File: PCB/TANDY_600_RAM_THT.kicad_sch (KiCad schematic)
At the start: 5 parts, among them J1 DIN 41612 2x22 male right-ang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, U1 628128, U2 74HC08

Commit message: dual_008
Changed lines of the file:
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@@
   )
   (label "A16" (at 140.97 109.22 0)
-    (effects (font (size 1.524 1.524)) (justify left bottom))
+    (effects (font (size 1.27 1.27)) (justify left bottom))
   )
   (label "A14" (at 66.04 58.42 180)
@@
   )
   (label "A15" (at 140.97 96.52 0)
-    (effects (font (size 1.524 1.524)) (justify left bottom))
+    (effects (font (size 1.27 1.27)) (justify left bottom))
   )
   (label "D3" (at 209.55 66.04 0)

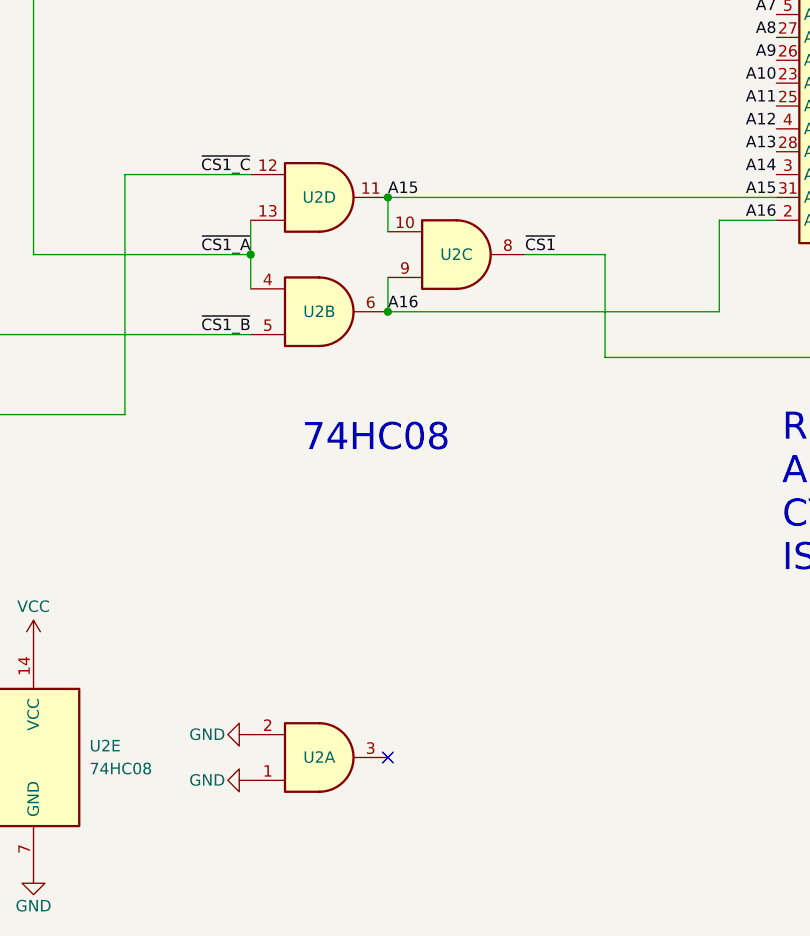
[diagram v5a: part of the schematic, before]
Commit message: dual version add /CE pullup for battery life
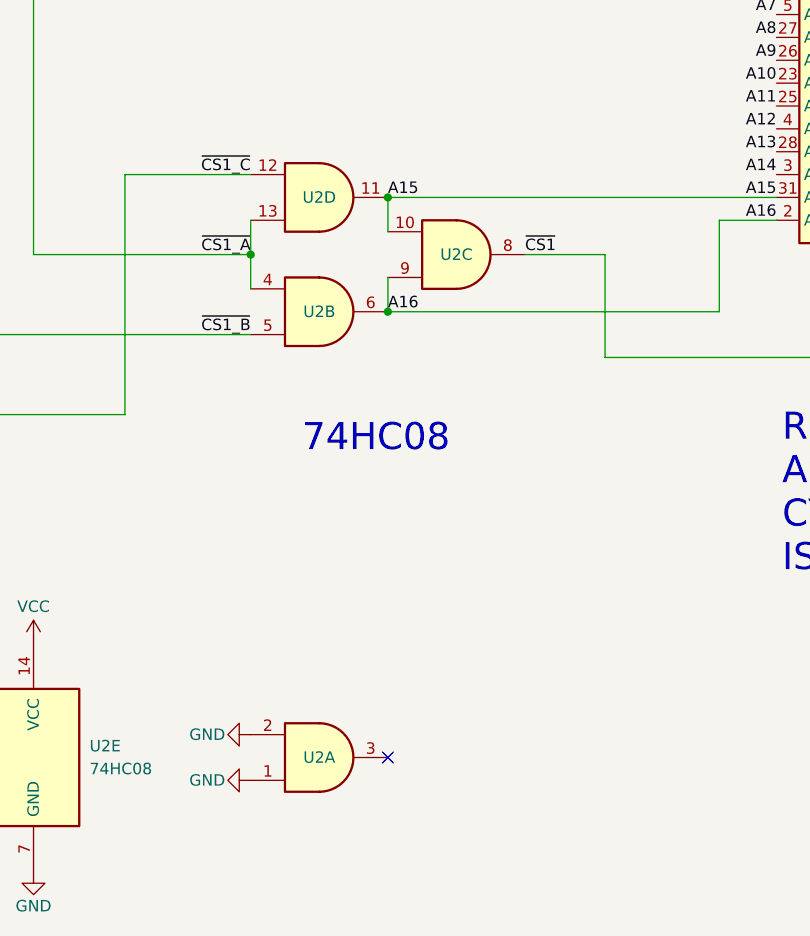
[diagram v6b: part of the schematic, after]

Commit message: datasheets OPRM pinout
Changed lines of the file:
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@@
 (kicad_sch
-	(version 20231120)
+	(version 20250114)
 	(generator "eeschema")
-	(generator_version "8.0")
+	(generator_version "9.0")
 	(paper "USLetter")
 	(title_block
@@
 		(comment 3 "Replaces TANDY Cat. No. 26-3910 \"OPRM\"")
 	)
+	(text "~{RAM_BACKUP}"
+		(exclude_from_sim no)
+		(at 83.82 101.6 0)
+		(effects
+			(font
+				(size 1.27 1.27)
+			)
+			(justify left bottom)
+		)
+	)
+	(text "74HC08"
+		(exclude_from_sim no)
+		(at 131.445 125.095 0)
+		(effects
+			(font
+				(size 3 3)
+			)
+			(justify left bottom)
+		)
+	)
+	(text "R1LP0108E\nAS6C1008\nCY62128ELL\nIS62C1024AL\n"
+		(exclude_from_sim no)
+		(at 184.785 138.43 0)
+		(effects
+			(font
+				(size 3 3)
+			)
+			(justify left bottom)
+		)
+	)
 	(junction
 		(at 125.73 102.87)
@@
 		)
 	)
-	(text "~{RAM_BACKUP}"
-		(exclude_from_sim no)
-		(at 83.82 101.6 0)
-		(effects
-			(font
-				(size 1.27 1.27)
-			)
-			(justify left bottom)
-		)
-	)
-	(text "74HC08"
-		(exclude_from_sim no)
-		(at 131.445 125.095 0)
-		(effects
-			(font
-				(size 3 3)
-			)
-			(justify left bottom)
-		)
-	)
-	(text "R1LP0108E\nAS6C1008\nCY62128ELL\nIS62C1024AL\n"
-		(exclude_from_sim no)
-		(at 184.785 138.43 0)
-		(effects
-			(font
-				(size 3 3)
-			)
-			(justify left bottom)
-		)
-	)
 	(label "D2"
 		(at 78.74 88.9 0)
-		(fields_autoplaced yes)
 		(effects
 			(font
@@
 	(label "~{CS1_C}"
 		(at 66.04 99.06 180)
-		(fields_autoplaced yes)
 		(effects
 			(font
@@
 	(label "A13"
 		(at 78.74 58.42 0)
-		(fields_autoplaced yes)
 		(effects
 			(font
@@
 	(label "A12"
 		(at 66.04 60.96 180)
-		(fields_autoplaced yes)
 		(effects
 			(font
@@
 	(label "D6"
 		(at 66.04 83.82 180)
-		(fields_autoplaced yes)
 		(effects
 			(font
@@
 	(label "A13"
 		(at 184.15 91.44 180)
-		(fields_autoplaced yes)
 		(effects
 			(font
@@
 	(label "A7"
 		(at 184.15 76.2 180)
-		(fields_autoplaced yes)
 		(effects
 			(font
@@
 	(label "A1"
 		(at 184.15 60.96 180)
-		(fields_autoplaced yes)
 		(effects
 			(font
@@
 	(label "~{WE}"
 		(at 209.55 88.9 0)
-		(fields_autoplaced yes)
 		(effects
 			(font
@@
 	(label "A4"
 		(at 66.04 73.66 180)
-		(fields_autoplaced yes)
 		(effects
 			(font
@@
 	(label "A3"
 		(at 66.04 76.2 180)
-		(fields_autoplaced yes)
 		(effects
 			(font
@@
 	(label "A4"
 		(at 184.15 68.58 180)
-		(fields_autoplaced yes)
 		(effects
 			(font
@@
 	(label "A12"
 		(at 184.15 88.9 180)
-		(fields_autoplaced yes)
 		(effects
 			(font
@@
 	(label "A9"
 		(at 184.15 81.28 180)
-		(fields_autoplaced yes)
 		(effects
 			(font
@@
 	(label "D0"
 		(at 209.55 58.42 0)
-		(fields_autoplaced yes)
 		(effects
 			(font
@@
 	(label "D0"
 		(at 78.74 91.44 0)
-		(fields_autoplaced yes)
 		(effects
 			(font
@@
 	(label "D7"
 		(at 78.74 81.28 0)
-		(fields_autoplaced yes)
 		(effects
 			(font
@@
 	(label "CS2"
 		(at 78.74 101.6 0)
-		(fields_autoplaced yes)
 		(effects
 			(font
@@
 	(label "A2"
 		(at 78.74 76.2 0)
-		(fields_autoplaced yes)
 		(effects
 			(font
@@
 	(label "D5"
 		(at 209.55 71.12 0)
-		(fields_autoplaced yes)
 		(effects
 			(font
@@
 	(label "A5"
 		(at 184.15 71.12 180)
-		(fields_autoplaced yes)
 		(effects
 			(font
@@
 	(label "A1"
 		(at 66.04 78.74 180)
-		(fields_autoplaced yes)
 		(effects
 			(font
@@
 	(label "~{CS1_A}"
 		(at 78.74 55.88 0)
-		(fields_autoplaced yes)
 		(effects
 			(font
@@
 	(label "CS2"
 		(at 209.55 83.82 0)
-		(fields_autoplaced yes)
 		(effects
 			(font
@@
 	(label "D4"
 		(at 66.04 86.36 180)
-		(fields_autoplaced yes)
 		(effects
 			(font
@@
 	(label "A11"
 		(at 184.15 86.36 180)
-		(fields_autoplaced yes)
 		(effects
 			(font
@@
 	(label "A16"
 		(at 184.15 99.06 180)
-		(fields_autoplaced yes)
 		(effects
 			(font
@@
 	(label "D1"
 		(at 66.04 91.44 180)
-		(fields_autoplaced yes)
 		(effects
 			(font
@@
 	(label "A10"
 		(at 184.15 83.82 180)
-		(fields_autoplaced yes)
 		(effects
 			(font
@@
 	(label "A3"
 		(at 184.15 66.04 180)
-		(fields_autoplaced yes)
 		(effects
 			(font
@@
 	(label "~{CS1}"
 		(at 156.21 102.87 0)
-		(fields_autoplaced yes)
 		(effects
 			(font
@@
 	(label "~{CS1_B}"
 		(at 78.74 99.06 0)
-		(fields_autoplaced yes)
 		(effects
 			(font
@@
 	(label "D5"
 		(at 78.74 83.82 0)
-		(fields_autoplaced yes)
 		(effects
 			(font
@@
 	(label "~{CS1_B}"
 		(at 125.73 111.76 180)
-		(fields_autoplaced yes)
 		(effects
 			(font
@@
 	(label "A6"
 		(at 66.04 71.12 180)
-		(fields_autoplaced yes)
 		(effects
 			(font
@@
 	(label "A5"
 		(at 78.74 71.12 0)
-		(fields_autoplaced yes)
 		(effects
 			(font
@@
 	(label "~{OE}"
 		(at 78.74 93.98 0)
-		(fields_autoplaced yes)
 		(effects
 			(font
@@
 	(label "A0"
 		(at 78.74 78.74 0)
-		(fields_autoplaced yes)
 		(effects
 			(font
@@
 	(label "A8"
 		(at 78.74 66.04 0)
-		(fields_autoplaced yes)
 		(effects
 			(font
@@
 	(label "~{CS1_C}"
 		(at 125.73 93.98 180)
-		(fields_autoplaced yes)
 		(effects
 			(font
@@
 	(label "D1"
 		(at 209.55 60.96 0)
-		(fields_autoplaced yes)
 		(effects
 			(font
@@
 	(label "D3"
 		(at 66.04 88.9 180)
-		(fields_autoplaced yes)
 		(effects
 			(font
@@
 	(label "A14"
 		(at 184.15 93.98 180)
-		(fields_autoplaced yes)
 		(effects
 			(font
@@
 	(label "A10"
 		(at 78.74 63.5 0)
-		(fields_autoplaced yes)
 		(effects
 			(font
@@
 	(label "A11"
 		(at 66.04 63.5 180)
-		(fields_autoplaced yes)
 		(effects
 			(font
@@
 	(label "A2"
 		(at 184.15 63.5 180)
-		(fields_autoplaced yes)
 		(effects
 			(font
@@
 	(label "D7"
 		(at 209.55 76.2 0)
-		(fields_autoplaced yes)
 		(effects
 			(font
@@
 	(label "A16"
 		(at 140.97 109.22 0)
-		(fields_autoplaced yes)
 		(effects
 			(font
@@
 	(label "A14"
 		(at 66.04 58.42 180)
-		(fields_autoplaced yes)
 		(effects
 			(font
@@
 	(label "~{CS1_A}"
 		(at 125.73 102.87 180)
-		(fields_autoplaced yes)
 		(effects
 			(font
@@
 	(label "A8"
 		(at 184.15 78.74 180)
-		(fields_autoplaced yes)
 		(effects
 			(font
@@
 	(label "D2"
 		(at 209.55 63.5 0)
-		(fields_autoplaced yes)
 		(effects
 			(font
@@
 	(label "A15"
 		(at 140.97 96.52 0)
-		(fields_autoplaced yes)
 		(effects
 			(font
@@
 	(label "D3"
 		(at 209.55 66.04 0)
-		(fields_autoplaced yes)
 		(effects
 			(font
@@
 	(label "A7"
 		(at 78.74 68.58 0)
-		(fields_autoplaced yes)
 		(effects
 			(font
@@
 	(label "A15"
 		(at 184.15 96.52 180)
-		(fields_autoplaced yes)
 		(effects
 			(font
@@
 	(label "A0"
 		(at 184.15 58.42 180)
-		(fields_autoplaced yes)
 		(effects
 			(font
@@
 	(label "A9"
 		(at 66.04 66.04 180)
-		(fields_autoplaced yes)
 		(effects
 			(font
@@
 	(label "~{OE}"
 		(at 209.55 86.36 0)
-		(fields_autoplaced yes)
 		(effects
 			(font
@@
 	(label "A6"
 		(at 184.15 73.66 180)
-		(fields_autoplaced yes)
 		(effects
 			(font
@@
 	(label "~{CS1}"
 		(at 209.55 81.28 0)
-		(fields_autoplaced yes)
 		(effects
 			(font
@@
 	(label "D4"
 		(at 209.55 68.58 0)
-		(fields_autoplaced yes)
 		(effects
 			(font
@@
 	(label "D6"
 		(at 209.55 73.66 0)
-		(fields_autoplaced yes)
 		(effects
 			(font
@@
 	(label "~{WE}"
 		(at 78.74 96.52 0)
-		(fields_autoplaced yes)
 		(effects
 			(font
@@
 			)
 		)
-		(property "Datasheet" "~"
+		(property "Datasheet" "datasheets/TANDY_600_OPRM.pdf"
 			(at 71.12 76.2 0)
 			(effects
@@
 		)
 	)
+	(embedded_fonts no)
 )
